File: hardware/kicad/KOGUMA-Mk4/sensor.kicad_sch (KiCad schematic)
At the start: 42 parts, among them J5 ENC_L, J6 ENC_R, U70 NJU6080, U71 NJU6080, U72 NJU6080, U73 NJU6080, U74 OPA2354, U75 OPA2354, U76 LSM6DSR

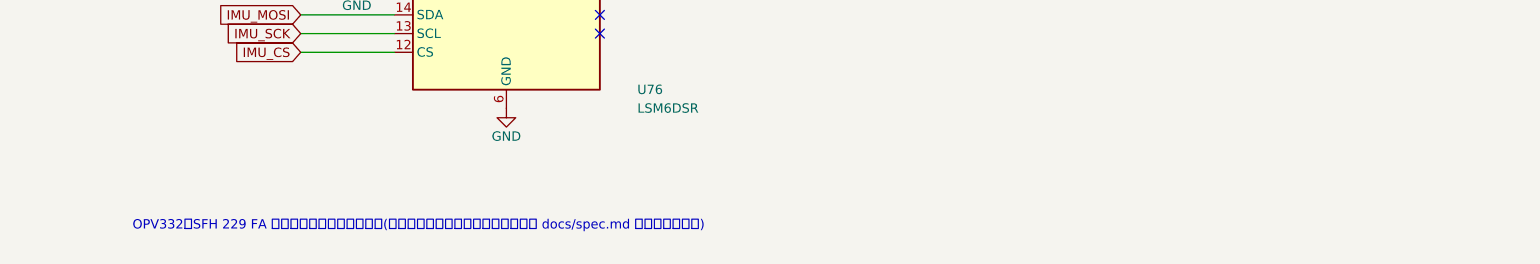
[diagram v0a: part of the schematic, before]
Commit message: 基板 v7: 形をすっきりさせ、壁センサをホルダに入れる(ToraNeko.Mk3 と同じ形)
- mechanical/sensor_holder: センサのホルダ v1(CadQuery、STEP・STL)。ToraNeko の
  センサホルダ v4 の STEP を測った寸法(6.0 x 4.04 x 10.5mm、φ3.2 の穴を 3.5・8.1mm、
  3 x 3mm のほぞ)。上に発光 OPV332、下に受光 SFH 229 FA
- 基板 v7(pcb_shape.py): 後ろは長方形、前はセンサを囲む凸の形をフレームの 1mm 内側で
  切り、車輪の所と前の腕の間だけへこませる。角は R3。ほぞの穴を外形に入れた
- 壁センサの位置: 前 (12, ±30) → (18, ±29)、横 (41, ±24) → (41, ±18.5)。向きは同じ
- フットプリント WallSensor_Holder_Emitter / Receiver を作り、D70〜D77 に割り当てた
- 機体: 54.95g、272 g·cm²、ぶつかりなし。基板の1次の振動 166Hz(ホルダの重さで 203 → 166Hz)
- エンコーダ基板のモデルを 5.3 x 12.3mm(穴を通す形)に合わせた

Co-Authored-By: Claude Opus 5.5 <noreply@anthropic.com>
Claude-Session: https://claude.ai/code/session_01H2Zvpqxqu2v63zaiCMmfT3
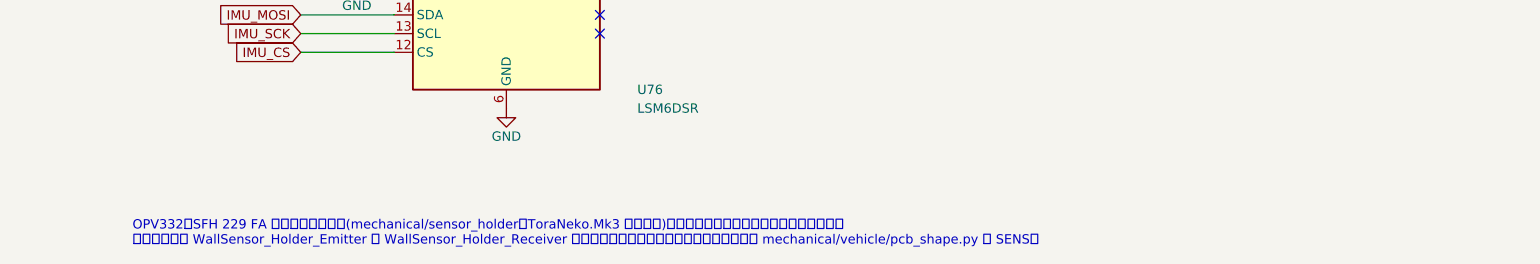
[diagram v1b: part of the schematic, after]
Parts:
- D70, D71, D72, D73: footprint (none) -> KOGUMA-Mk4:WallSensor_Holder_Emitter
- D74, D75, D76, D77: footprint (none) -> KOGUMA-Mk4:WallSensor_Holder_Receiver
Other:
- note added: "OPV332・SFH 229 FA はセンサのホルダ(mechanical/sensor_holder、ToraNeko.Mk3 と同じ形)に入れる。発光が上の穴、受光が下の穴。 同じセンサの WallSensor_Holder_Emitter と WallSensor_Holder_Receiver は同じ位置・同じ向きに置く。位置と向きは mechanical/vehicle/pcb_shape.py の SENS。"
- note removed: "OPV332・SFH 229 FA のフットプリントは未作成(基板の上に寝かせる。位置と向きは docs/spec.md の「壁センサ」)"
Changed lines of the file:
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@@
 			)
 		)
-		(property "Footprint" ""
+		(property "Footprint" "KOGUMA-Mk4:WallSensor_Holder_Emitter"
 			(at 83.82 69.85 90)
 			(effects
@@
 			)
 		)
-		(property "Footprint" ""
+		(property "Footprint" "KOGUMA-Mk4:WallSensor_Holder_Emitter"
 			(at 170.18 69.85 90)
 			(effects
@@
 			)
 		)
-		(property "Footprint" ""
+		(property "Footprint" "KOGUMA-Mk4:WallSensor_Holder_Emitter"
 			(at 256.54 69.85 90)
 			(effects
@@
 			)
 		)
-		(property "Footprint" ""
+		(property "Footprint" "KOGUMA-Mk4:WallSensor_Holder_Emitter"
 			(at 342.9 69.85 90)
 			(effects
@@
 			)
 		)
-		(property "Footprint" ""
+		(property "Footprint" "KOGUMA-Mk4:WallSensor_Holder_Receiver"
 			(at 27.94 152.4 90)
 			(effects
@@
 			)
 		)
-		(property "Footprint" ""
+		(property "Footprint" "KOGUMA-Mk4:WallSensor_Holder_Receiver"
 			(at 121.92 152.4 90)
 			(effects
@@
 			)
 		)
-		(property "Footprint" ""
+		(property "Footprint" "KOGUMA-Mk4:WallSensor_Holder_Receiver"
 			(at 215.9 152.4 90)
 			(effects
@@
 			)
 		)
-		(property "Footprint" ""
+		(property "Footprint" "KOGUMA-Mk4:WallSensor_Holder_Receiver"
 			(at 309.88 152.4 90)
 			(effects
@@
 		)
 	)
-	(text "OPV332・SFH 229 FA のフットプリントは未作成(基板の上に寝かせる。位置と向きは docs/spec.md の「壁センサ」)"
+	(text "OPV332・SFH 229 FA はセンサのホルダ(mechanical/sensor_holder、ToraNeko.Mk3 と同じ形)に入れる。発光が上の穴、受光が下の穴。\n同じセンサの WallSensor_Holder_Emitter と WallSensor_Holder_Receiver は同じ位置・同じ向きに置く。位置と向きは mechanical/vehicle/pcb_shape.py の SENS。"
 		(exclude_from_sim no)
 		(at 25.4 276.86 0)

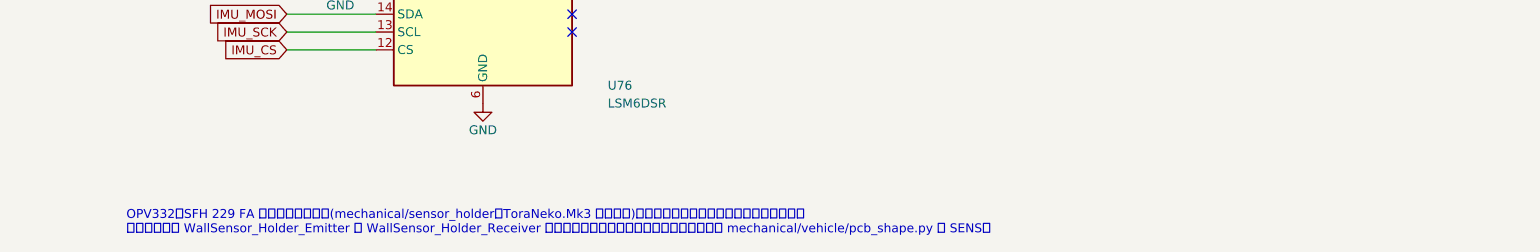
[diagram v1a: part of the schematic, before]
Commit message: 壁センサのホルダを基板の裏に付ける(ホルダ v2)
- ホルダを基板の下にさかさまに付ける。ToraNeko と同じ高さ(10.5mm)ではフレームまで
  0.1mm なので、高さ 9.9mm、穴を基板から 3.2(受光)・7.6mm(発光)にした(フレームまで 0.7mm)
- 光の高さは受光 z 10.4、発光 z 6.0。機体で光を遮る部品がないことを確かめた
- 機体: 54.88g、重心の高さ z 12.71(13.02 から)、271 g·cm²、ぶつかりなし。基板の1次の振動 169Hz
- フットプリントの説明を「裏の面に置く」に。外形 v7 はそのまま

Co-Authored-By: Claude Opus 5.5 <noreply@anthropic.com>
Claude-Session: https://claude.ai/code/session_01H2Zvpqxqu2v63zaiCMmfT3
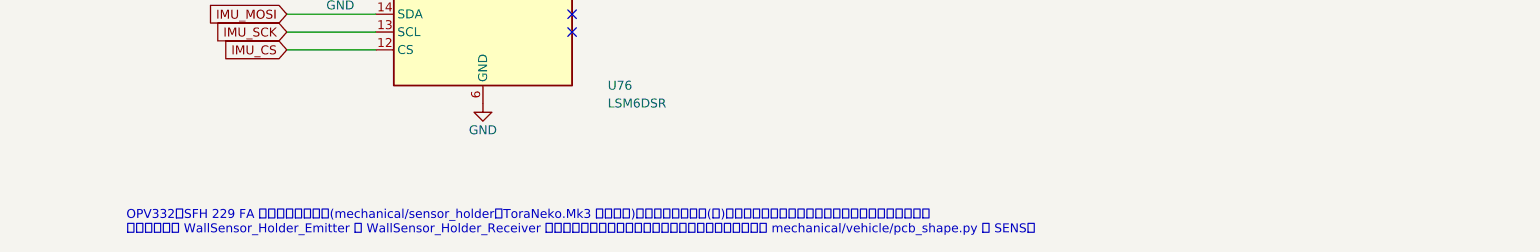
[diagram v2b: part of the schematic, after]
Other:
- note added: "OPV332・SFH 229 FA はセンサのホルダ(mechanical/sensor_holder、ToraNeko.Mk3 と同じ形)に入れ、基板の裏(下)に付ける。発光が基板から遠い穴、受光が近い穴。 同じセンサの WallSensor_Holder_Emitter と WallSensor_Holder_Receiver は裏の面に、同じ位置・同じ向きに置く。位置と向きは mechanical/vehicle/pcb_shape.py の SENS。"
- note removed: "OPV332・SFH 229 FA はセンサのホルダ(mechanical/sensor_holder、ToraNeko.Mk3 と同じ形)に入れる。発光が上の穴、受光が下の穴。 同じセンサの WallSensor_Holder_Emitter と WallSensor_Holder_Receiver は同じ位置・同じ向きに置く。位置と向きは mechanical/vehicle/pcb_shape.py の SENS。"
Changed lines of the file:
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@@
 		)
 	)
-	(text "OPV332・SFH 229 FA はセンサのホルダ(mechanical/sensor_holder、ToraNeko.Mk3 と同じ形)に入れる。発光が上の穴、受光が下の穴。\n同じセンサの WallSensor_Holder_Emitter と WallSensor_Holder_Receiver は同じ位置・同じ向きに置く。位置と向きは mechanical/vehicle/pcb_shape.py の SENS。"
+	(text "OPV332・SFH 229 FA はセンサのホルダ(mechanical/sensor_holder、ToraNeko.Mk3 と同じ形)に入れ、基板の裏(下)に付ける。発光が基板から遠い穴、受光が近い穴。\n同じセンサの WallSensor_Holder_Emitter と WallSensor_Holder_Receiver は裏の面に、同じ位置・同じ向きに置く。位置と向きは mechanical/vehicle/pcb_shape.py の SENS。"
 		(exclude_from_sim no)
 		(at 25.4 276.86 0)

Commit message: IMU の INT1 を MCU の PD2 につなぐ(IMU_INT、データ準備完了の割り込み)
回路図(MCU・センサのシート)、docs/pinmap.md、check_pins.py を更新。使う45本、残り1本(PB3)

Co-Authored-By: Claude Opus 5.5 <noreply@anthropic.com>
Claude-Session: https://claude.ai/code/session_01H2Zvpqxqu2v63zaiCMmfT3
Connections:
- net IMU_INT: now reaches U76.4 (INT1)
- no-connect marks 4 -> 3
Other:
- note added: "IMU: LSM6DSR を SPI(SPI3、モード3)で。SDX・SCX は GND。INT1 は MCU の PD2(IMU_INT、データ準備完了の割り込み。2026-10-31)。INT2 はつながない。"
- note removed: "IMU: LSM6DSR を SPI(SPI3、モード3)で。SDX・SCX は GND。INT1・INT2 は今はつながない(PD2 が空いている)。"
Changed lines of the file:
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@@
 		)
 	)
-	(no_connect
-		(at 91.44 238.76)
+	(wire
+		(pts
+			(xy 91.44 238.76) (xy 96.52 238.76)
+		)
+		(stroke
+			(width 0)
+			(type default)
+		)
+	)
+	(global_label "IMU_INT"
+		(shape output)
+		(at 96.52 238.76 0)
+		(fields_autoplaced yes)
+		(effects
+			(font
+				(size 1.27 1.27)
+			)
+			(justify left)
+		)
+		(property "Intersheetrefs" "${INTERSHEET_REFS}"
+			(at 96.52 238.76 0)
+			(effects
+				(font
+					(size 1.27 1.27)
+				)
+				(hide yes)
+			)
+		)
 	)
 	(no_connect
@@
 		)
 	)
-	(text "IMU: LSM6DSR を SPI(SPI3、モード3)で。SDX・SCX は GND。INT1・INT2 は今はつながない(PD2 が空いている)。"
+	(text "IMU: LSM6DSR を SPI(SPI3、モード3)で。SDX・SCX は GND。INT1 は MCU の PD2(IMU_INT、データ準備完了の割り込み。2026-10-31)。INT2 はつながない。"
 		(exclude_from_sim no)
 		(at 25.4 210.82 0)

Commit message: SW1・SW2・BZ1 のフットプリントを作り、NJU6080 を SOT-23-6 に。全部の部品にフットプリントが付いた
寸法はメーカーの推奨ランド: SSSS810701(Alps の Land Dimensions)、TVAF06-A020B-R(仕様書の
P.C.B LAND DIMENSION)、SMT-0540-S-R(Suggested Land Pattern)。gen_footprints.py で作る。ERC エラー 0

Co-Authored-By: Claude Opus 5.5 <noreply@anthropic.com>
Claude-Session: https://claude.ai/code/session_01H2Zvpqxqu2v63zaiCMmfT3
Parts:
- U70, U71, U72, U73: footprint (none) -> Package_TO_SOT_SMD:SOT-23-6
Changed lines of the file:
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@@
 			)
 		)
-		(property "Footprint" ""
+		(property "Footprint" "Package_TO_SOT_SMD:SOT-23-6"
 			(at 50.8 71.12 0)
 			(effects
@@
 			)
 		)
-		(property "Footprint" ""
+		(property "Footprint" "Package_TO_SOT_SMD:SOT-23-6"
 			(at 137.16 71.12 0)
 			(effects
@@
 			)
 		)
-		(property "Footprint" ""
+		(property "Footprint" "Package_TO_SOT_SMD:SOT-23-6"
 			(at 223.52 71.12 0)
 			(effects
@@
 			)
 		)
-		(property "Footprint" ""
+		(property "Footprint" "Package_TO_SOT_SMD:SOT-23-6"
 			(at 309.88 71.12 0)
 			(effects
